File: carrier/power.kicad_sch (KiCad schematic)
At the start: 27 parts, among them U5 MAX1709

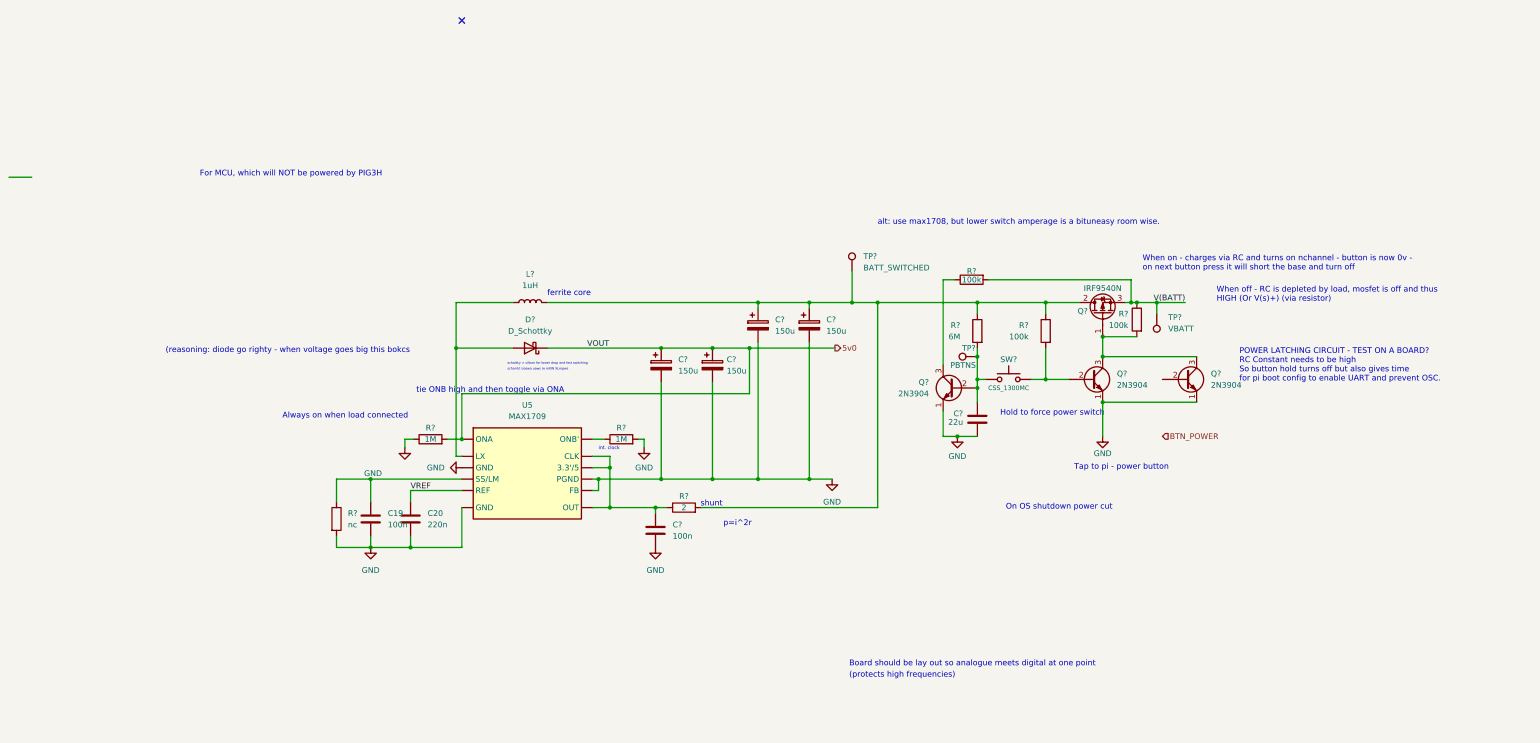
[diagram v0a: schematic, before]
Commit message: fixed switching and added fuel gague
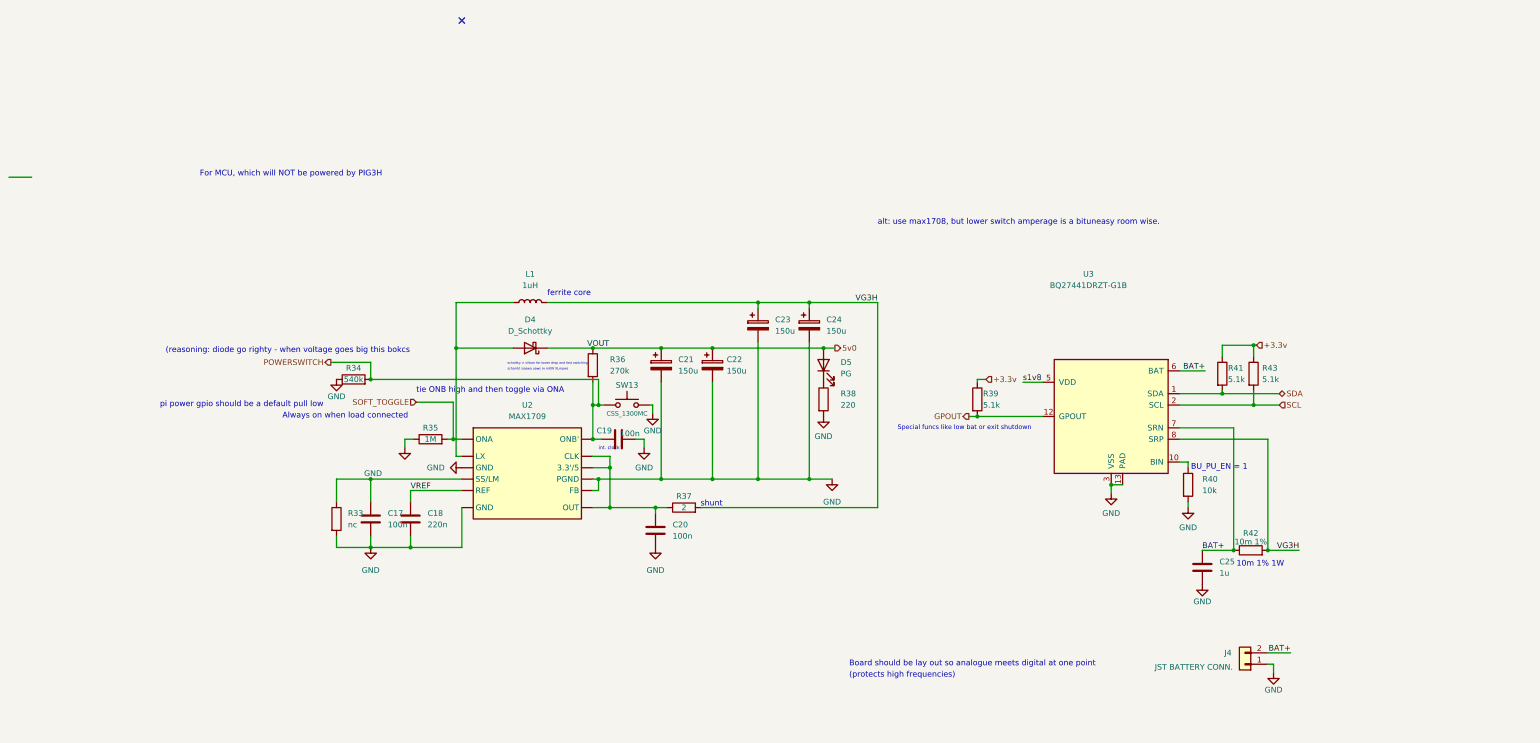
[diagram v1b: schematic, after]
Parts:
- removed C?: 22u, symbol Device:C
- removed Q? (x3): 2N3904, Package_TO_SOT_THT:TO-92_Inline, symbol Transistor_BJT:2N3904
- removed Q?: IRF9540N, Package_TO_SOT_THT:TO-220-3_Vertical, symbol Transistor_FET:IRF9540N
- removed R? (x3): 100k, symbol Device:R
- removed R?: 6M, symbol Device:R
- removed R?: 1M, symbol Device:R
- removed SW?: CSS_1300MC, symbol Switch:SW_Push
- removed TP?: BATT_SWITCHED, symbol Connector:TestPoint
- removed TP?: PBTNS, symbol Connector:TestPoint
- removed TP?: VBATT, symbol Connector:TestPoint
- added C19: 100n, symbol Device:C
- added C25: 1u, symbol Device:C
- added D5: PG, symbol Device:LED
- added J4: JST BATTERY CONN., Connector_JST:JST_XH_B2B-XH-AM_1x02_P2.50mm_Vertical, symbol Connector_Generic:Conn_01x02
- added R34: 540k, symbol Device:R
- added R36: 270k, symbol Device:R
- added R38: 220, symbol Device:R
- added R39, R41, R43: 5.1k, symbol Device:R
- added R40: 10k, symbol Device:R
- added R42: 10m 1%, symbol Device:R
- added SW13: CSS_1300MC, symbol Switch:SW_Push
- added U3: BQ27441DRZT-G1B, Package_SON:Texas_S-PDSO-N12, symbol Battery_Management:BQ27441DRZT-G1B
- gave numbers to parts that had none: 10
- renumbered C19 to C17, C20 to C18, U5 to U2
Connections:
- net 5v0: now also D5.2 (A), R36.1; no longer R35.2, U2. (SS/LM)
- net GND: now also C19.2, C25.2, J4.1 (Pin_1), R34.1, R38.2, R40.2, SW13.1, U3.13 (PAD), U3.3 (VSS)
- net VG3H: now reaches C23.1, C24.1, L1.2, R37.2
- net VG3H: now also R42.2, U3.8 (SRP)
- new net: R40.1, U3.10 (BIN)
- new net: D5.1 (K), R38.1
- new net +3.3v: R39.1, R41.1, R43.1
- new net BAT+: C25.1, J4.2 (Pin_2), R42.1, U3.6 (BAT), U3.7 (SRN)
- new net GPOUT: R39.2, U3.12 (GPOUT)
- new net POWERSWITCH: C19.1, R34.2, R36.2, SW13.2, U2. (SS/LM)
- new net SCL: R43.2, U3.2 (SCL)
- new net SDA: R41.2, U3.1 (SDA)
- new net SOFT_TOGGLE: R35.2, U2. (SS/LM)
- new net s1v8: U3.5 (VDD)
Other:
- note added: "10m 1% 1W"
- note added: "BU_PU_EN = 1"
- note added: "Special funcs like low bat or exit shutdown"
- note added: "pi power gpio should be a default pull low"
- note removed: "Hold to force power switch"
- note removed: "On OS shutdown power cut"
- note removed: "POWER LATCHING CIRCUIT - TEST ON A BOARD? RC Constant needs to be high So button hold turns off but also gives time for pi boot config to enable UART and prevent OSC."
- note removed: "Tap to pi - power button"
- note removed: "When off - RC is depleted by load, mosfet is off and thus HIGH (Or V(s)+) (via resistor)"
- note removed: "When on - charges via RC and turns on nchannel - button is now 0v - on next button press it will short the base and turn off"
- note removed: "p=i^2r"

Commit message: need to finish footprint assignments then can do rev2 pcb (cooler one)
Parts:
- D4: footprint (none) -> Package_TO_SOT_SMD:TO-252-2
- L1: footprint (none) -> Inductor_SMD:L_Sumida_CDMC6D28_7.25x6.5mm

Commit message: new footprints - order stuff soon
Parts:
- removed SW13: CSS_1300MC, symbol Switch:SW_Push
- added SW13: SW_SPDT, CM4IO:SS3HVB, symbol Switch:SW_SPDT
- D4: renamed from D5; footprint (none) -> LED_SMD:LED_0603_1608Metric_Pad1.05x0.95mm_HandSolder
- R32: renamed from R33; footprint (none) -> Resistor_SMD:R_0603_1608Metric_Pad0.98x0.95mm_HandSolder
- R33: renamed from R34; footprint (none) -> Resistor_SMD:R_0603_1608Metric_Pad0.98x0.95mm_HandSolder
- R34: renamed from R35; footprint (none) -> Resistor_SMD:R_0603_1608Metric_Pad0.98x0.95mm_HandSolder
- R35: renamed from R36; footprint (none) -> Resistor_SMD:R_0603_1608Metric_Pad0.98x0.95mm_HandSolder
- R37: renamed from R38; footprint (none) -> Resistor_SMD:R_0603_1608Metric_Pad0.98x0.95mm_HandSolder
- R38: renamed from R39; footprint (none) -> Resistor_SMD:R_0603_1608Metric_Pad0.98x0.95mm_HandSolder
- R39: renamed from R40; footprint (none) -> Resistor_SMD:R_0603_1608Metric_Pad0.98x0.95mm_HandSolder
- R40: renamed from R41; footprint (none) -> Resistor_SMD:R_0603_1608Metric_Pad0.98x0.95mm_HandSolder
- R42: renamed from R43; footprint (none) -> Resistor_SMD:R_0603_1608Metric_Pad0.98x0.95mm_HandSolder
- renumbered D4 to D3, R37 to R36, R42 to R41
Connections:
- net GND: now also SW13.C1 (B)
- net POWERSWITCH: now also SW13.B1 (C)
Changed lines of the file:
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@@
-    (stroke (width 0) (type default) (color 0 0 0 0))
-  )
-  (wire (pts (xy 131.445 103.505) (xy 131.445 101.6))
-    (stroke (width 0) (type default) (color 0 0 0 0))
-  )
-  (wire (pts (xy 131.445 101.6) (xy 130.81 101.6))
     (stroke (width 0) (type default) (color 0 0 0 0))
   )
@@
     (stroke (width 0) (type default) (color 0 0 0 0))
   )
+  (wire (pts (xy 118.11 101.6) (xy 119.38 101.6))
+    (stroke (width 0) (type default) (color 0 0 0 0))
+  )
   (wire (pts (xy 119.38 101.6) (xy 120.65 101.6))
     (stroke (width 0) (type default) (color 0 0 0 0))
   )
-  (wire (pts (xy 118.11 101.6) (xy 119.38 101.6))
-    (stroke (width 0) (type default) (color 0 0 0 0))
-  )
   (wire (pts (xy 68.58 92.075) (xy 59.69 92.075))
     (stroke (width 0) (type default) (color 0 0 0 0))
@@
   )
   (wire (pts (xy 248.92 101.6) (xy 265.43 101.6))
+    (stroke (width 0) (type default) (color 0 0 0 0))
+  )
+  (wire (pts (xy 130.81 99.06) (xy 131.445 99.06))
+    (stroke (width 0) (type default) (color 0 0 0 0))
+  )
+  (wire (pts (xy 131.445 99.06) (xy 131.445 103.505))
     (stroke (width 0) (type default) (color 0 0 0 0))
   )
@@
   (symbol (lib_id "Device:D_Schottky") (at 104.14 88.9 180) (unit 1)
     (in_bom yes) (on_board yes) (fields_autoplaced)
-    (property "Reference" "D4" (id 0) (at 104.14 82.55 0))
+    (property "Reference" "D3" (id 0) (at 104.14 82.55 0))
     (property "Value" "D_Schottky" (id 1) (at 104.14 85.09 0))
     (property "Footprint" "Package_TO_SOT_SMD:TO-252-2" (id 2) (at 104.14 88.9 0)
@@
   (symbol (lib_id "Device:R") (at 138.43 124.46 90) (unit 1)
     (in_bom yes) (on_board yes)
-    (property "Reference" "R37" (id 0) (at 138.43 121.92 90))
+    (property "Reference" "R36" (id 0) (at 138.43 121.92 90))
     (property "Value" "2" (id 1) (at 138.43 124.46 90))
     (property "Footprint" "" (id 2) (at 138.43 126.238 90)
@@
     )
     (pin "1")
+  )
+  (symbol (lib_id "Switch:SW_SPDT") (at 125.73 99.06 0) (mirror y) (unit 1)
+    (in_bom yes) (on_board yes)
+    (property "Reference" "SW13" (id 0) (at 127 101.6 0))
+    (property "Value" "SW_SPDT" (id 1) (at 127 103.505 0))
+    (property "Footprint" "CM4IO:SS3HVB" (id 2) (at 125.73 99.06 0)
+      (effects (font (size 1.27 1.27)) hide)
+    )
+    (property "Datasheet" "~" (id 3) (at 125.73 99.06 0)
+      (effects (font (size 1.27 1.27)) hide)
+    )
+    (pin "A1")
+    (pin "C1")
+    (pin "B1")
   )
   (symbol (lib_id "Battery_Management:BQ27441DRZT-G1B") (at 233.68 104.14 0) (mirror y) (unit 1)
@@
   (symbol (lib_id "Device:R") (at 203.835 100.33 0) (unit 1)
     (in_bom yes) (on_board yes)
-    (property "Reference" "R39" (id 0) (at 205.105 99.06 0)
+    (property "Reference" "R38" (id 0) (at 205.105 99.06 0)
       (effects (font (size 1.27 1.27)) (justify left))
     )
@@
       (effects (font (size 1.27 1.27)) (justify left))
     )
-    (property "Footprint" "" (id 2) (at 202.057 100.33 90)
+    (property "Footprint" "Resistor_SMD:R_0603_1608Metric_Pad0.98x0.95mm_HandSolder" (id 2) (at 202.057 100.33 90)
       (effects (font (size 1.27 1.27)) hide)
     )
@@
   (symbol (lib_id "Device:R") (at 64.77 95.885 90) (unit 1)
     (in_bom yes) (on_board yes)
-    (property "Reference" "R34" (id 0) (at 64.77 93.345 90))
+    (property "Reference" "R33" (id 0) (at 64.77 93.345 90))
     (property "Value" "540k" (id 1) (at 64.77 95.885 90))
-    (property "Footprint" "" (id 2) (at 64.77 97.663 90)
+    (property "Footprint" "Resistor_SMD:R_0603_1608Metric_Pad0.98x0.95mm_HandSolder" (id 2) (at 64.77 97.663 90)
       (effects (font (size 1.27 1.27)) hide)
     )
@@
   (symbol (lib_id "Device:R") (at 169.545 100.33 0) (unit 1)
     (in_bom yes) (on_board yes) (fields_autoplaced)
-    (property "Reference" "R38" (id 0) (at 173.355 99.0599 0)
+    (property "Reference" "R37" (id 0) (at 173.355 99.0599 0)
       (effects (font (size 1.27 1.27)) (justify left))
     )
@@
       (effects (font (size 1.27 1.27)) (justify left))
     )
-    (property "Footprint" "" (id 2) (at 167.767 100.33 90)
+    (property "Footprint" "Resistor_SMD:R_0603_1608Metric_Pad0.98x0.95mm_HandSolder" (id 2) (at 167.767 100.33 90)
       (effects (font (size 1.27 1.27)) hide)
     )
@@
   )
   (symbol (lib_id "Device:R") (at 118.11 92.71 0) (unit 1)
-    (in_bom yes) (on_board yes) (fields_autoplaced)
-    (property "Reference" "R36" (id 0) (at 121.92 91.4399 0)
-      (effects (font (size 1.27 1.27)) (justify left))
-    )
-    (property "Value" "270k" (id 1) (at 121.92 93.9799 0)
-      (effects (font (size 1.27 1.27)) (justify left))
-    )
-    (property "Footprint" "" (id 2) (at 116.332 92.71 90)
+    (in_bom yes) (on_board yes)
+    (property "Reference" "R35" (id 0) (at 120.65 91.44 0)
+      (effects (font (size 1.27 1.27)) (justify left))
+    )
+    (property "Value" "270k" (id 1) (at 120.65 93.98 0)
+      (effects (font (size 1.27 1.27)) (justify left))
+    )
+    (property "Footprint" "Resistor_SMD:R_0603_1608Metric_Pad0.98x0.95mm_HandSolder" (id 2) (at 116.332 92.71 90)
       (effects (font (size 1.27 1.27)) hide)
     )
@@
   (symbol (lib_id "Device:R") (at 60.96 127 0) (unit 1)
     (in_bom yes) (on_board yes) (fields_autoplaced)
-    (property "Reference" "R33" (id 0) (at 63.5 125.7299 0)
+    (property "Reference" "R32" (id 0) (at 63.5 125.7299 0)
       (effects (font (size 1.27 1.27)) (justify left))
     )
@@
       (effects (font (size 1.27 1.27)) (justify left))
     )
-    (property "Footprint" "" (id 2) (at 59.182 127 90)
+    (property "Footprint" "Resistor_SMD:R_0603_1608Metric_Pad0.98x0.95mm_HandSolder" (id 2) (at 59.182 127 90)
       (effects (font (size 1.27 1.27)) hide)
     )
     (property "Datasheet" "~" (id 3) (at 60.96 127 0)
-      (effects (font (size 1.27 1.27)) hide)
-    )
-    (pin "1")
-    (pin "2")
-  )
-  (symbol (lib_id "Switch:SW_Push") (at 125.73 101.6 0) (mirror y) (unit 1)
-    (in_bom yes) (on_board yes)
-    (property "Reference" "SW13" (id 0) (at 125.73 97.155 0))
-    (property "Value" "CSS_1300MC" (id 1) (at 125.73 103.505 0)
-      (effects (font (size 1.016 1.016)))
-    )
-    (property "Footprint" "" (id 2) (at 125.73 96.52 0)
-      (effects (font (size 1.27 1.27)) hide)
-    )
-    (property "Datasheet" "~" (id 3) (at 125.73 96.52 0)
       (effects (font (size 1.27 1.27)) hide)
     )
@@
   (symbol (lib_id "Device:R") (at 264.795 133.985 90) (unit 1)
     (in_bom yes) (on_board yes)
-    (property "Reference" "R42" (id 0) (at 264.795 130.175 90))
+    (property "Reference" "R41" (id 0) (at 264.795 130.175 90))
     (property "Value" "10m 1%" (id 1) (at 264.795 132.08 90))
     (property "Footprint" "" (id 2) (at 264.795 135.763 90)
@@
   (symbol (lib_id "Device:R") (at 250.825 119.38 0) (unit 1)
     (in_bom yes) (on_board yes) (fields_autoplaced)
-    (property "Reference" "R40" (id 0) (at 254 118.1099 0)
+    (property "Reference" "R39" (id 0) (at 254 118.1099 0)
       (effects (font (size 1.27 1.27)) (justify left))
     )
@@
       (effects (font (size 1.27 1.27)) (justify left))
     )
-    (property "Footprint" "" (id 2) (at 249.047 119.38 90)
+    (property "Footprint" "Resistor_SMD:R_0603_1608Metric_Pad0.98x0.95mm_HandSolder" (id 2) (at 249.047 119.38 90)
       (effects (font (size 1.27 1.27)) hide)
     )
@@
   (symbol (lib_id "Device:R") (at 265.43 94.615 0) (unit 1)
     (in_bom yes) (on_board yes)
-    (property "Reference" "R43" (id 0) (at 267.335 93.345 0)
+    (property "Reference" "R42" (id 0) (at 267.335 93.345 0)
       (effects (font (size 1.27 1.27)) (justify left))
     )
@@
       (effects (font (size 1.27 1.27)) (justify left))
     )
-    (property "Footprint" "" (id 2) (at 263.652 94.615 90)
+    (property "Footprint" "Resistor_SMD:R_0603_1608Metric_Pad0.98x0.95mm_HandSolder" (id 2) (at 263.652 94.615 90)
       (effects (font (size 1.27 1.27)) hide)
     )
@@
   (symbol (lib_id "Device:R") (at 81.915 109.22 90) (unit 1)
     (in_bom yes) (on_board yes)
-    (property "Reference" "R35" (id 0) (at 81.915 106.68 90))
+    (property "Reference" "R34" (id 0) (at 81.915 106.68 90))
     (property "Value" "1M" (id 1) (at 81.915 109.22 90))
-    (property "Footprint" "" (id 2) (at 81.915 110.998 90)
+    (property "Footprint" "Resistor_SMD:R_0603_1608Metric_Pad0.98x0.95mm_HandSolder" (id 2) (at 81.915 110.998 90)
       (effects (font (size 1.27 1.27)) hide)
     )
@@
   (symbol (lib_id "Device:LED") (at 169.545 92.71 90) (unit 1)
     (in_bom yes) (on_board yes)
-    (property "Reference" "D5" (id 0) (at 173.355 92.075 90)
+    (property "Reference" "D4" (id 0) (at 173.355 92.075 90)
       (effects (font (size 1.27 1.27)) (justify right))
     )
@@
       (effects (font (size 1.27 1.27)) (justify right))
     )
-    (property "Footprint" "" (id 2) (at 169.545 92.71 0)
+    (property "Footprint" "LED_SMD:LED_0603_1608Metric_Pad1.05x0.95mm_HandSolder" (id 2) (at 169.545 92.71 0)
       (effects (font (size 1.27 1.27)) hide)
     )
@@
   (symbol (lib_id "Device:R") (at 258.445 94.615 0) (unit 1)
     (in_bom yes) (on_board yes)
-    (property "Reference" "R41" (id 0) (at 259.715 93.345 0)
+    (property "Reference" "R40" (id 0) (at 259.715 93.345 0)
       (effects (font (size 1.27 1.27)) (justify left))
     )
@@
       (effects (font (size 1.27 1.27)) (justify left))
     )
-    (property "Footprint" "" (id 2) (at 256.667 94.615 90)
-      (effects (font (size 1.27 1.27)) hide)
-    )
+    (property "Footprint" "Resistor_SMD:R_0603_1608Metric_Pad0.98x0.95mm_HandSolder" (id 2) (at 256.667 94.615 90)
+      (effects (font (size 1.27 1.27)) hide)
+    )

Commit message: aaa
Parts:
- added U?: MAX77751, symbol CM4IO:MAX77751
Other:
- note removed: "For MCU, which will NOT be powered by PIG3H"
- note removed: "alt: use max1708, but lower switch amperage is a bituneasy room wise."
- moved on the sheet: C17, C18, C19, C20, C21, C22, C23, C24, C25, D3, D4, L1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

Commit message: thing
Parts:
- removed U3: BQ27441DRZT-G1B, Package_SON:Texas_S-PDSO-N12, symbol Battery_Management:BQ27441DRZT-G1B
- added C?: 470n, symbol Device:C
- added U?: BQ27441DRZT-G1B, Package_SON:Texas_S-PDSO-N12, symbol Battery_Management:BQ27441DRZT-G1B
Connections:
- net BAT+: now also R41.2, U?.10 (VDD), U?.13 (BATT), U?.14 (BATT), U?.6 (BAT), U?.7 (SRN); no longer R41.1
- net GND: now also U?.9 (GND), C?.2, U?.13 (PAD), U?.3 (VSS)
- net GPOUT: now also U?.12 (GPOUT)
- net SDA: now also U?.1 (SDA)
- net VG3H: now also R41.1, U?.8 (SRP); no longer R41.2
- net VBUS: now reaches U?.23 (CHGIN)
- net VBUS: now also U?.24 (CHGIN)
- net CC2: now reaches U?.4 (CC2)
- net CC1: now reaches U?.5 (CC1)
- net DP: now reaches U?.6 (DP)
- net DN: now reaches U?.7 (DN)
- net at R39.1: now also U?.10 (BIN)
- new net: C?.1, U?.5 (VDD)
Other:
- moved on the sheet: C25, J4, R38, R39, R40, R41, R42, U?

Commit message: chrgere
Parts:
- added C?: 10u, symbol Device:C
- added D? (x2): LED, symbol Device:LED
- added R? (x2): R, symbol Device:R
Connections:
- net BAT+: now also C?.1; no longer U?.10 (VDD)
- net GND: now also U?.18 (PGND), U?.19 (PGND), U?.8 (ENBST), C?.2
- net VG3H: now also U?.15 (SYS), U?.16 (SYS), D?.2 (A), D?.2 (A); no longer R41.1, U?.8 (SRP)
- net at U?.2 (INOKB): now also R?.2
- net at U?.3 (STAT): now also R?.2
- new net: R41.1, U?.10 (VDD), U?.8 (SRP)
- new net: D?.1 (K), R?.1 (x2)
- no-connect marks 1 -> 0
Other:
- note added: "1W"
- note added: "Boost Converter (V(batt) --> 5v)"
- note removed: "10m 1% 1W"
- moved on the sheet: C17, C18, C19, C20, C21, C22, C23, C24, C25, C?, D3, D4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
